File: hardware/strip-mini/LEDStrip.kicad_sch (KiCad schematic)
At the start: 9 parts, among them U201 74AHC1G125

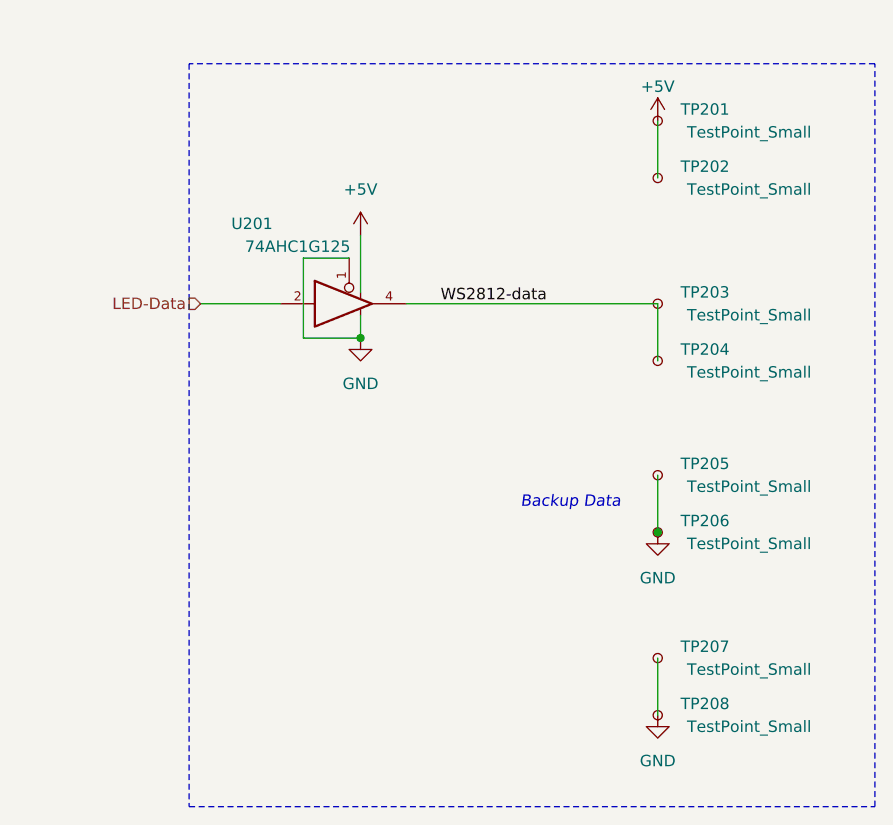
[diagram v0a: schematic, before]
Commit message: Replace Order_Number
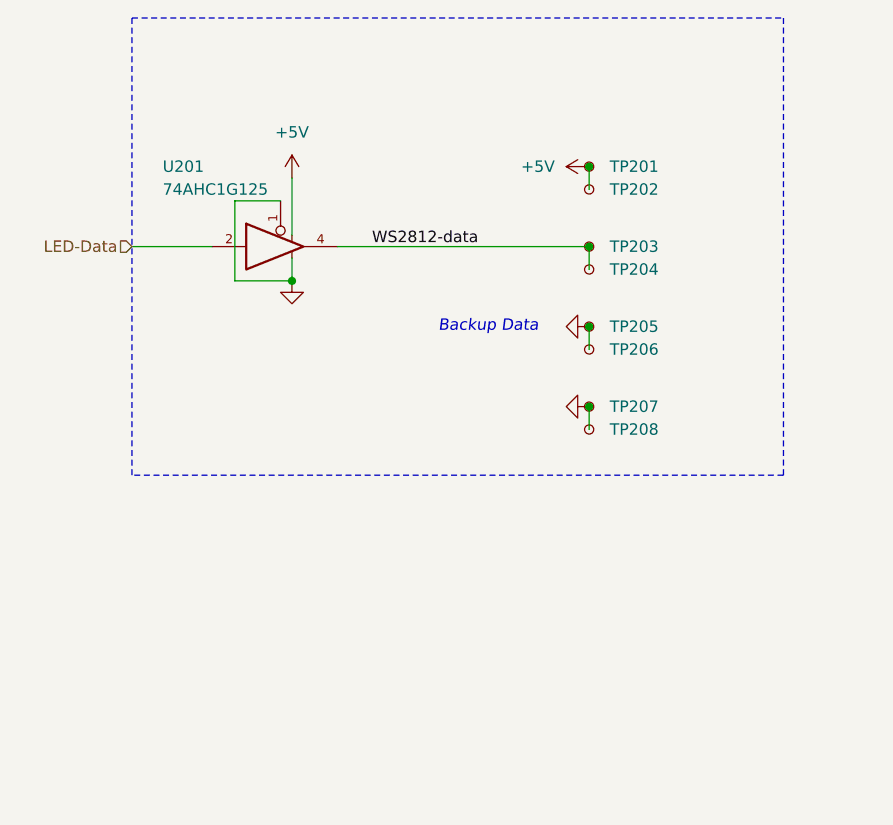
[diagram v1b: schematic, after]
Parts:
- removed TP202, TP204, TP205, TP207: TestPoint_Small, V2_TestPoint:TestPoint_Pad_2.0x2.0mm, symbol Connector:TestPoint_Small
- added TP202, TP204, TP206, TP208: ~, V2_TestPoint:TestPoint_Pad_2.0x2.0mm, symbol V2_Connector:TestPoint_Pad_2.0x2.0mm
- TP201, TP203: value TestPoint_Small -> ~; symbol Connector:TestPoint_Small -> V2_Connector:TestPoint_Pad_2.0x2.0mm; now left out of the parts list
- TP205: renamed from TP206; value TestPoint_Small -> ~; symbol Connector:TestPoint_Small -> V2_Connector:TestPoint_Pad_2.0x2.0mm; now left out of the parts list
- TP207: renamed from TP208; value TestPoint_Small -> ~; symbol Connector:TestPoint_Small -> V2_Connector:TestPoint_Pad_2.0x2.0mm; now left out of the parts list
- U201: footprint Package_TO_SOT_SMD:SOT-23-5 -> V2_Package_TO_SOT_SMD:SOT-23-5; Manufacturer (none) -> Texas Instruments; Mouser (none) -> 595-SN74AHC1G125DBVR; Product (none) -> SN74AHC1G125DBVR
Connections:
- net +5V: now also TP202.1
- net GND: now also TP206.1, TP208.1
- net WS2812-data: now also TP204.1
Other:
- moved on the sheet: TP201, TP203, TP205, TP207, U201

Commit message: Update
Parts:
- TP201, TP202, TP203, TP204, TP205, TP206, TP207, TP208: value ~ -> (none); Id (none) -> Connector:${SYMBOL_NAME}
- U201: Id (none) -> 74xGxx:${SYMBOL_NAME}; Rating (none) -> 8mA
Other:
- title: LED Strip -> V2 strip mini
